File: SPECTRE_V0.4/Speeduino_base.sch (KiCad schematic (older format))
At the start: 160 parts, among them IC1 LM340?-MP, Q1 2N7002, Q10 BSP78, Q11 BSP78, Q12 BSP78, Q13 BSP78, Q2 CJ2302, Q3 CJ2302, Q4 CJ2302, Q5 BSP78, Q6 BSP78, Q7 CJ2302, Q8 CJ2302, Q9 CJ2302, U1 MAX9926UAEE+, U2 molex_48pin

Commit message: Cleaned up V0.4 Bug fixes in board V0.4 Changed readme to add more to be tested functions
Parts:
- removed L1: 470R-2A, Speeduino_base:L0805, symbol Speeduino_base-eagle-import:SMD-FERRITE-BEAD-470R-2A(0805)'0805'
- added D22, D23, D24, D25: 1N4007, Diode_SMD:D_SOD-128, symbol Device:D_Small
- added J1: Conn_01x04_Male, Connector_PinHeader_2.54mm:PinHeader_1x04_P2.54mm_Vertical, symbol Connector:Conn_01x04_Male
- added R72: 0R0, Resistor_SMD:R_0603_1608Metric_Pad1.05x0.95mm_HandSolder, symbol Speeduino_base-eagle-import:SMD-RES-470R-5%-1_10W(0603)
- added R73, R74: 1k, Speeduino_base:R0603, symbol Speeduino_base-eagle-import:SMD-RES-470R-5%-1_10W(0603)
- R69: value 1k -> 180
- R70: value 1k -> 82
- R71: value 1k -> 560
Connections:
- wire segments 540 -> 548
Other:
- moved on the sheet: D1, D4, R13, R4

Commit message: Lots of changes, started new PCB with 8 inj channels.
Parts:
- removed F3, F4: PPTC 16V2A, Speeduino_base:1812L, symbol Speeduino_base-eagle-import:?1812L
- removed F5, F6, F7: PPTC 16V2A, Fuse:Fuse_1812_4532Metric, symbol Device:Polyfuse_Small
- removed IC1: LM340?-MP, Speeduino_base:SOT223, symbol Speeduino_base-eagle-import:LM340?-MP
- removed JP15, JP5, JP6, JP7, JP8: SolderJumper_3_Bridged12, Jumper:SolderJumper-3_P1.3mm_Bridged12_Pad1.0x1.5mm, symbol Jumper:SolderJumper_3_Bridged12
- removed U$1: A4988BREAKOUT, Speeduino_base:A4988BREAKOUT, symbol Speeduino_base-eagle-import:A4988BREAKOUT
- added A1: Pololu_Breakout_DRV8825, Module:Pololu_Breakout-16_15.2x20.3mm, symbol Driver_Motor:Pololu_Breakout_DRV8825
- added D26: 1N4007, Diode_SMD:D_SOD-128, symbol Device:D_Small
- added F2: PPTC 16V2A, Resistor_SMD:R_1812_4532Metric_Pad1.30x3.40mm_HandSolder, symbol Speeduino_base-eagle-import:?1812L
- added Q14, Q15, Q16, Q17, Q18: BSP78, Speeduino_base:SOT223, symbol Speeduino_base-eagle-import:NMOSSOT223
- added R75, R76: 10k, Resistor_SMD:R_0603_1608Metric_Pad1.05x0.95mm_HandSolder, symbol Device:R_Small
- added R77: 100, Speeduino_base:R0603, symbol Speeduino_base-eagle-import:SMD-RES-470R-5%-1_10W(0603)
- added R78, R79, R80, R81, R82: 10k, Speeduino_base:R0603, symbol Speeduino_base-eagle-import:SMD-RES-470R-5%-1_10W(0603)
- added U3: LM78M05_TO220, Package_TO_SOT_THT:TO-220-3_Vertical, symbol Regulator_Linear:LM78M05_TO220
- F1: footprint Speeduino_base:1812L -> Resistor_SMD:R_1812_4532Metric_Pad1.30x3.40mm_HandSolder
- J1: footprint Connector_PinHeader_2.54mm:PinHeader_1x04_P2.54mm_Vertical -> Connector_PinHeader_2.00mm:PinHeader_1x04_P2.00mm_Vertical_SMD_Pin1Left
- R2: footprint Speeduino_base:R0603 -> Resistor_SMD:R_0603_1608Metric_Pad1.05x0.95mm_HandSolder
- R23: footprint Speeduino_base:R-7,5 -> Varistor:RV_Disc_D12mm_W3.9mm_P7.5mm
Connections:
- net labels added: BOOST-OUT, INJ5-OUT, INJ6-OUT, INJ7-OUT, INJ8-OUT
- net labels removed: Baro, PA11, PA12, PA15, PA6, PA7, PB0, PC10, PC11, PC12, PC9, PD2, VREF+, VREF-, V_IGN, V_INJ12, V_INJ34, V_O2
- wire segments 548 -> 476
- no-connect marks 0 -> 50
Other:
- moved on the sheet: C1, C10, C12, C14, C15, C16, C17, C18, C19, C2, C20, C21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

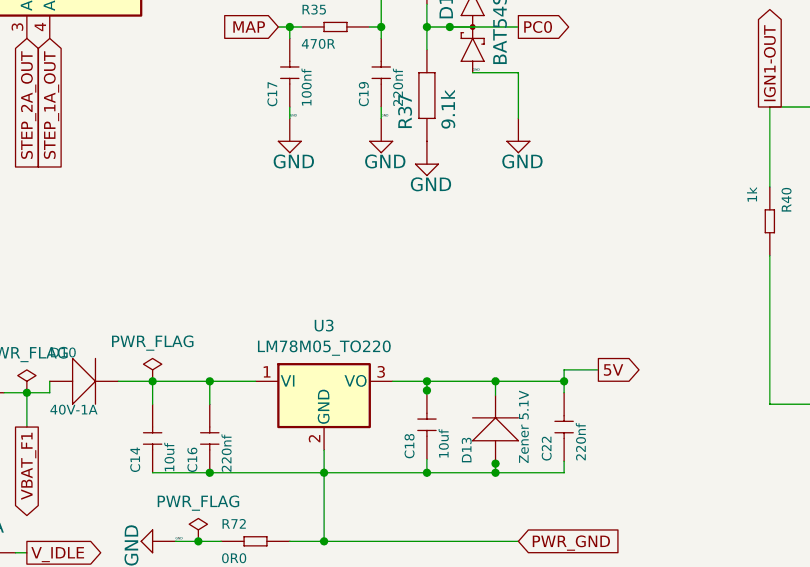
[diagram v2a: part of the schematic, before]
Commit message: Add zener for safety on 3.3v. All bat54S diodes dump current on 3.3V line when driven above 3.6V therefor the 3.3V needed protection
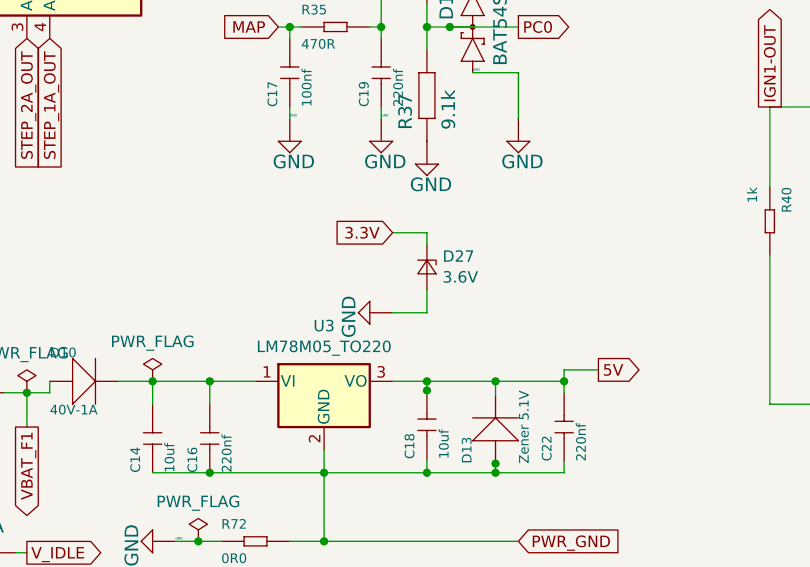
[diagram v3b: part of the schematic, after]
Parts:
- added D27: 3.6V, Diode_SMD:D_MiniMELF_Handsoldering, symbol Device:D_Zener_Small
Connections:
- wire segments 476 -> 480
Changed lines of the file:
@@
 Text GLabel 11750 3400 0    50   BiDi ~ 0
 PB7
-Text GLabel 11750 3500 0    50   BiDi ~ 0
-PB5
 Text GLabel 11750 3600 0    50   BiDi ~ 0
 PD7
@@
 Text GLabel 12050 3400 2    50   BiDi ~ 0
 PB6
-Text GLabel 12050 3500 2    50   BiDi ~ 0
-PB3
 Text GLabel 12050 3600 2    50   BiDi ~ 0
 PD6
@@
 NoConn ~ 10500 4800
 NoConn ~ 10500 4900
+$Comp
+L Device:D_Zener_Small D27
+U 1 1 5E7D198A
+P 3150 10300
+F 0 "D27" V 3104 10368 50  0000 L CNN
+F 1 "3.6V" V 3195 10368 50  0000 L CNN
+F 2 "Diode_SMD:D_MiniMELF_Handsoldering" V 3150 10300 50  0001 C CNN
+F 3 "~" V 3150 10300 50  0001 C CNN
+	1    3150 10300
+	0    1    1    0
+$EndComp
+Wire Wire Line
+	3150 10200 3150 10150
+Wire Wire Line
+	3150 10150 3000 10150
+Wire Wire Line
+	3150 10400 3150 10500
+Wire Wire Line
+	3150 10500 3000 10500
+$Comp
+L Speeduino_base-eagle-import:GND #SUPPLY0108
+U 1 1 5E8517DF
+P 2900 10500
+F 0 "#SUPPLY0108" H 2900 10500 50  0001 C CNN
+F 1 "GND" H 2825 10375 59  0000 L BNN
+F 2 "" H 2900 10500 50  0001 C CNN
+F 3 "" H 2900 10500 50  0001 C CNN
+	1    2900 10500
+	0    1    1    0
+$EndComp
+Text GLabel 3000 10150 0    50   Input ~ 0
+3.3V
+Text GLabel 11750 3500 0    50   BiDi ~ 0
+PB5
+Text GLabel 12050 3500 2    50   BiDi ~ 0
+PB3
 $EndSCHEMATC

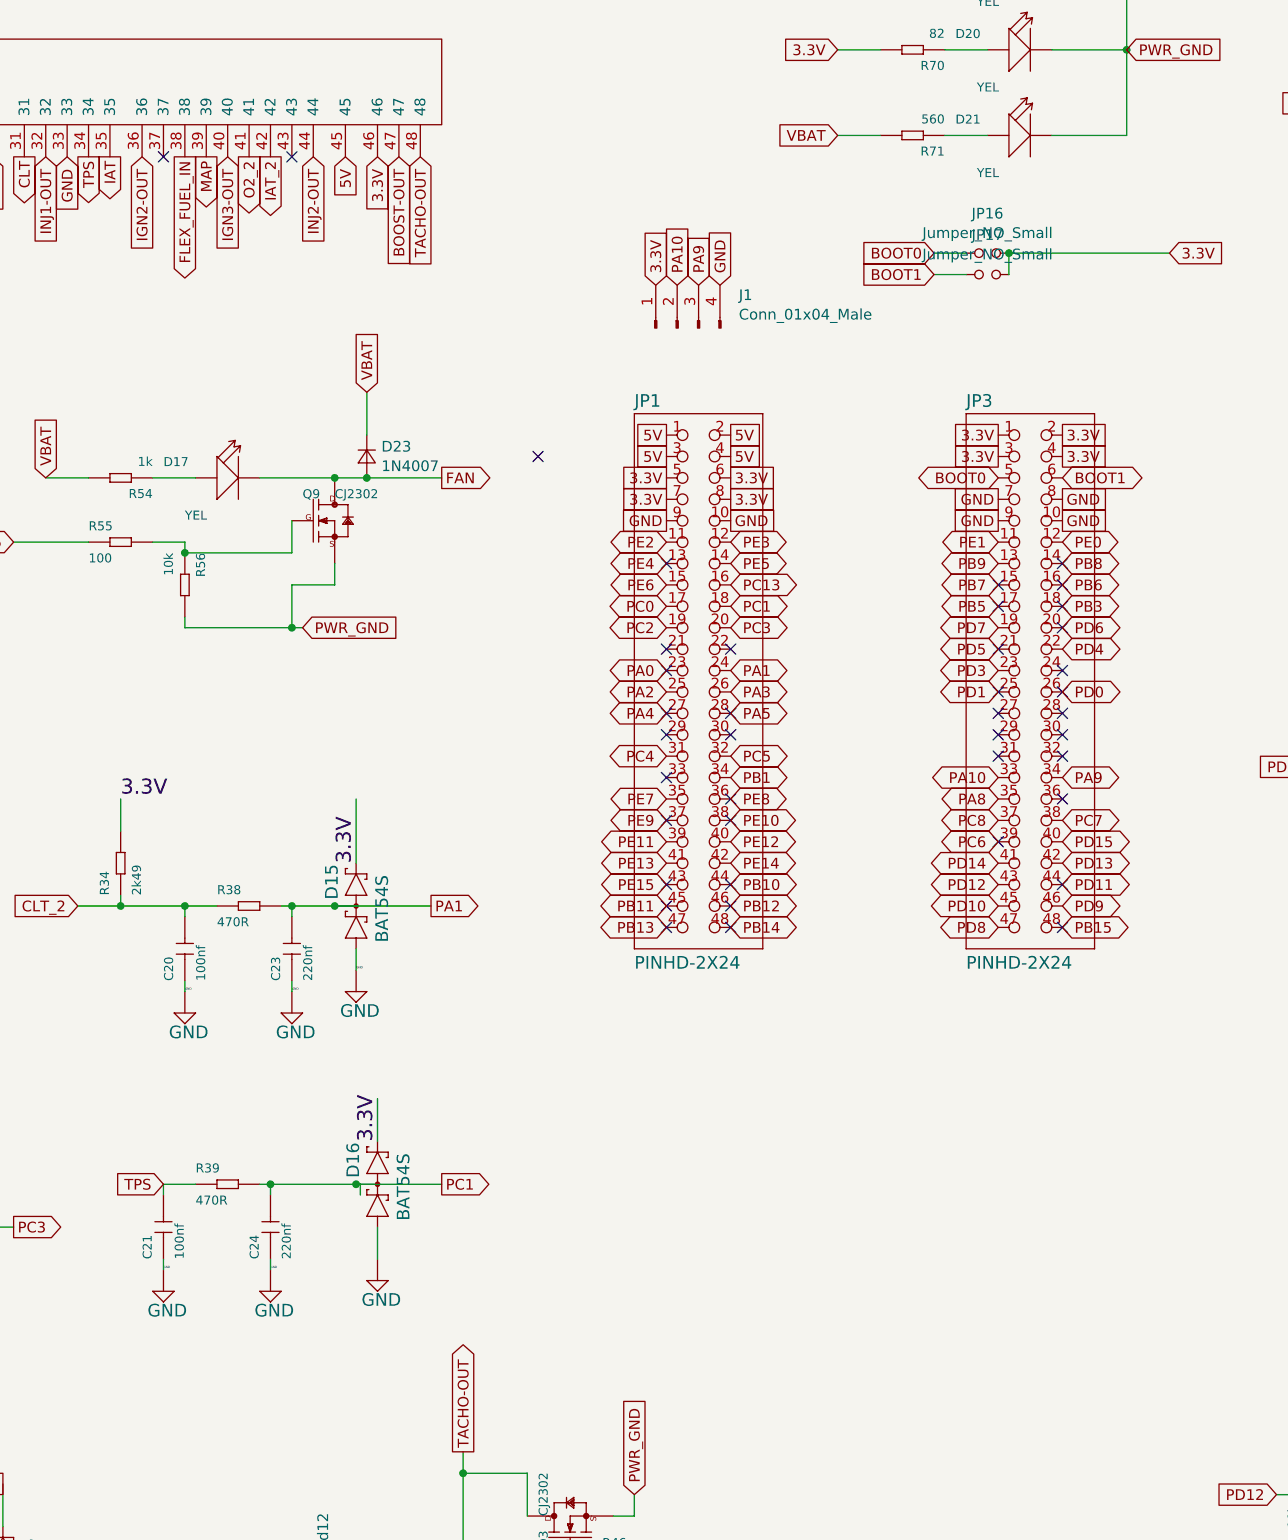
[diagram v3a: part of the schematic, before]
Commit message: add canbus driver add 3d models to components for 3d render.
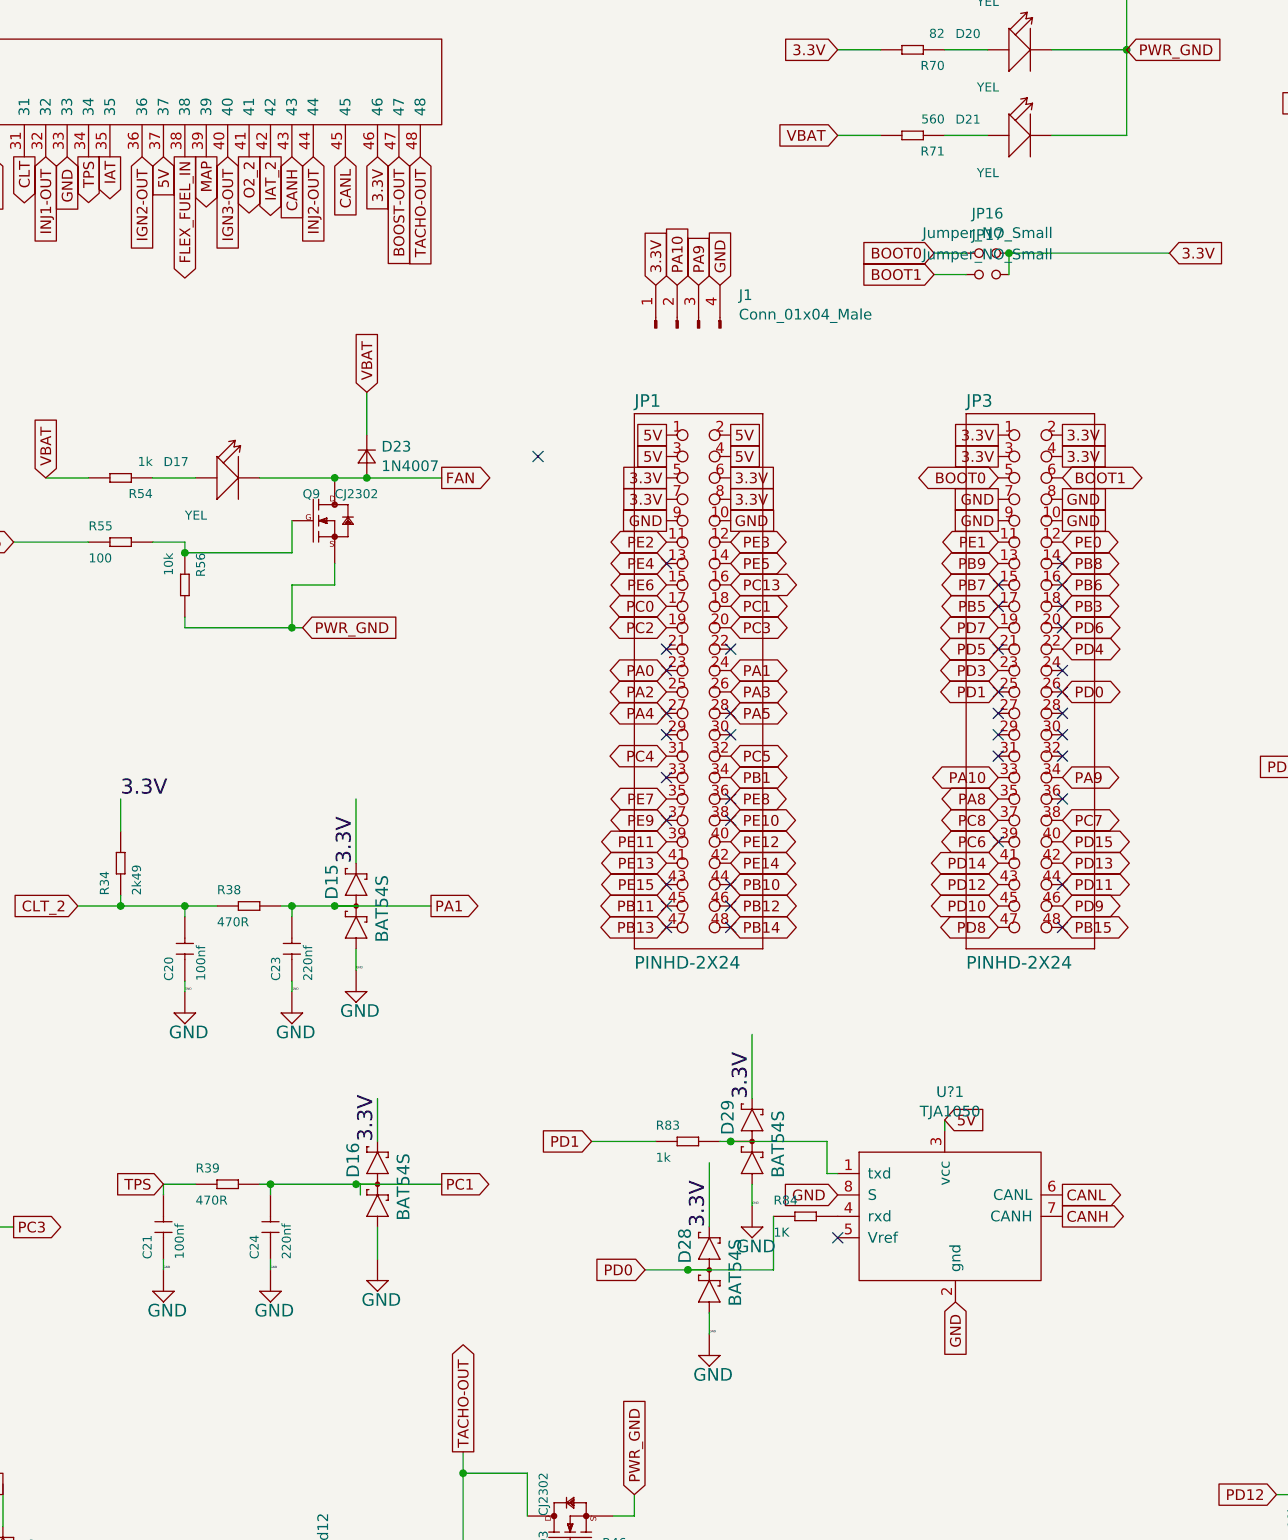
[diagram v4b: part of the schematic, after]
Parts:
- added D28, D29: BAT54S, Speeduino_base:SOT23, symbol Speeduino_base-eagle-import:BAT54S
- added R83: 1k, Speeduino_base:R0603, symbol Speeduino_base-eagle-import:SMD-RES-470R-5%-1_10W(0603)
- added R84: 1K, Speeduino_base:R0603, symbol Speeduino_base-eagle-import:SMD-RES-470R-5%-1_10W(0603)
- added U?1: TJA1050, Package_SO:SO-8_5.3x6.2mm_P1.27mm, symbol speeduino_lib:TJA1050
- D22, D23, D24, D25, D26: footprint Diode_SMD:D_SOD-128 -> Speeduino_base:D_SOD-128
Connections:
- net labels added: CANH, CANL
- wire segments 480 -> 493
- no-connect marks 50 -> 49
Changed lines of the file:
@@
-$EndComp
-$Comp
-L Speeduino_base-eagle-import:BAT54S D15
-U 1 1 20478EC3
-P 8750 4900
-F 0 "D15" H 8780 4979 59  0000 L BNN
-F 1 "BAT54S" H 8580 4744 59  0000 L BNN
-F 2 "Speeduino_base:SOT23" H 8750 4900 50  0001 C CNN
-F 3 "" H 8750 4900 50  0001 C CNN
-	1    8750 4900
-	0    -1   -1   0
 $EndComp
 $Comp
@@
 Text GLabel 5050 1400 3    50   Input ~ 0
 STEP_1B_OUT
-Text GLabel 8700 1400 3    50   Input ~ 0
+Text GLabel 7850 1400 3    50   Input ~ 0
 5V
 Text GLabel 8050 1400 3    50   Output ~ 0
 MAP
-Connection ~ 4200 1400
-$Comp
-L molex_48pin:molex_48pin U2
-U 1 1 5E17AB54
-P 6900 1950
-F 0 "U2" V 8187 2355 60  0000 C CNN
-F 1 "molex_48pin" V 8081 2355 60  0000 C CNN
-F 2 "rusefi_lib:Molex_48" H 6900 1950 60  0001 C CNN
-F 3 "" H 6900 1950 60  0001 C CNN
-	1    6900 1950
-	0    -1   -1   0
-$EndComp
 Text GLabel 7050 1400 3    50   Input ~ 0
 GND
@@
 F 0 "D24" V 14654 2418 50  0000 L CNN
 F 1 "1N4007" V 14745 2418 50  0000 L CNN
-F 2 "Diode_SMD:D_SOD-128" V 14700 2350 50  0001 C CNN
+F 2 "Speeduino_base:D_SOD-128" V 14700 2350 50  0001 C CNN
 F 3 "~" V 14700 2350 50  0001 C CNN
 	1    14700 2350
@@
 F 0 "D25" V 14654 3918 50  0000 L CNN
 F 1 "1N4007" V 14745 3918 50  0000 L CNN
-F 2 "Diode_SMD:D_SOD-128" V 14700 3850 50  0001 C CNN
+F 2 "Speeduino_base:D_SOD-128" V 14700 3850 50  0001 C CNN
 F 3 "~" V 14700 3850 50  0001 C CNN
 	1    14700 3850
@@
 F 0 "D22" V 5554 3368 50  0000 L CNN
 F 1 "1N4007" V 5645 3368 50  0000 L CNN
-F 2 "Diode_SMD:D_SOD-128" V 5600 3300 50  0001 C CNN
+F 2 "Speeduino_base:D_SOD-128" V 5600 3300 50  0001 C CNN
 F 3 "~" V 5600 3300 50  0001 C CNN
 	1    5600 3300
@@
 F 0 "D23" V 8754 2868 50  0000 L CNN
 F 1 "1N4007" V 8845 2868 50  0000 L CNN
-F 2 "Diode_SMD:D_SOD-128" V 8800 2800 50  0001 C CNN
+F 2 "Speeduino_base:D_SOD-128" V 8800 2800 50  0001 C CNN
 F 3 "~" V 8800 2800 50  0001 C CNN
 	1    8800 2800
@@
 F 0 "D26" V 14504 818 50  0000 L CNN
 F 1 "1N4007" V 14595 818 50  0000 L CNN
-F 2 "Diode_SMD:D_SOD-128" V 14550 750 50  0001 C CNN
+F 2 "Speeduino_base:D_SOD-128" V 14550 750 50  0001 C CNN
 F 3 "~" V 14550 750 50  0001 C CNN
 	1    14550 750
@@
 	1    0    0    -1
 $EndComp
-NoConn ~ 8450 1400
-NoConn ~ 7850 1400
 NoConn ~ 5750 1400
 NoConn ~ 10200 4000
@@
 Text GLabel 12050 3500 2    50   BiDi ~ 0
 PB3
+$Comp
+L speeduino_lib:TJA1050 U?1
+U 1 1 5E827D30
+P 11600 6400
+F 0 "U?1" H 11525 7031 50  0000 C CNN
+F 1 "TJA1050" H 11525 6940 50  0000 C CNN
+F 2 "Package_SO:SO-8_5.3x6.2mm_P1.27mm" H 11600 6400 50  0001 C CNN
+F 3 "" H 11600 6400 50  0001 C CNN
+	1    11600 6400
+	1    0    0    -1
+$EndComp
+NoConn ~ 11000 6450
+Text GLabel 12050 6250 2    50   Output ~ 0
+CANL
+Text GLabel 12050 6350 2    50   Output ~ 0
+CANH
+Connection ~ 4200 1400
+$Comp
+L molex_48pin:molex_48pin U2
+U 1 1 5E17AB54
+P 6900 1950
+F 0 "U2" V 8187 2355 60  0000 C CNN
+F 1 "molex_48pin" V 8081 2355 60  0000 C CNN
+F 2 "rusefi_lib:Molex_48" H 6900 1950 60  0001 C CNN
+F 3 "" H 6900 1950 60  0001 C CNN
+	1    6900 1950
+	0    -1   -1   0
+$EndComp
+Text GLabel 8450 1400 3    50   Input ~ 0
+CANH
+Text GLabel 8700 1400 3    50   Input ~ 0
+CANL
+Text GLabel 11500 5900 2    50   Input ~ 0
+5V
+Wire Wire Line
+	11500 5900 11500 5950
+Text GLabel 10100 6600 0    50   Input ~ 0
+PD0
+Text GLabel 9850 6000 0    50   Input ~ 0
+PD1
+Text GLabel 11550 6750 3    50   Input ~ 0
+GND
+Text GLabel 11000 6250 0    50   Input ~ 0
+GND
+Wire Wire Line
+	10600 6300 10600 6200
+Text Label 10600 6300 0    10   ~ 0
+GND
+Wire Wire Line
+	10600 5800 10600 5500
+Text Label 10600 5800 1    70   ~ 0
+3.3V
+$Comp
+L Speeduino_base-eagle-import:GND #SUPPLY0109
+U 1 1 5E8B962B
+P 10600 6400
+F 0 "#SUPPLY0109" H 10600 6400 50  0001 C CNN
+F 1 "GND" H 10525 6275 59  0000 L BNN
+F 2 "" H 10600 6400 50  0001 C CNN
+F 3 "" H 10600 6400 50  0001 C CNN
+	1    10600 6400
+	1    0    0    -1
+$EndComp
+Wire Wire Line
+	10950 6000 10950 6150
+Wire Wire Line
+	10950 6150 11000 6150
+Wire Wire Line
+	10400 6900 10400 6800
+Text Label 10400 6900 0    10   ~ 0
+GND
+Wire Wire Line
+	10400 6400 10400 6100
+Text Label 10400 6400 1    70   ~ 0
+3.3V
+$Comp
+L Speeduino_base-eagle-import:GND #SUPPLY0110
+U 1 1 5E93B03C
+P 10400 7000
+F 0 "#SUPPLY0110" H 10400 7000 50  0001 C CNN
+F 1 "GND" H 10325 6875 59  0000 L BNN
+F 2 "" H 10400 7000 50  0001 C CNN
+F 3 "" H 10400 7000 50  0001 C CNN
+	1    10400 7000
+	1    0    0    -1
+$EndComp
+$Comp
+L Speeduino_base-eagle-import:BAT54S D28
+U 1 1 5E93B042
+P 10400 6600
+F 0 "D28" H 10430 6679 59  0000 L BNN
+F 1 "BAT54S" H 10230 6444 59  0000 L BNN
+F 2 "Speeduino_base:SOT23" H 10400 6600 50  0001 C CNN
+F 3 "" H 10400 6600 50  0001 C CNN
+	1    10400 6600
+	0    -1   -1   0
+$EndComp
+Wire Wire Line
+	10100 6600 10300 6600
+Connection ~ 10300 6600
+$Comp
+L Speeduino_base-eagle-import:SMD-RES-470R-5%-1_10W(0603) R84
+U 1 1 5E97C8A6
+P 10850 6350
+F 0 "R84" H 10700 6400 42  0000 L BNN
+F 1 "1K" H 10700 6250 42  0000 L BNN
+F 2 "Speeduino_base:R0603" H 10850 6350 50  0001 C CNN
+F 3 "" H 10850 6350 50  0001 C CNN
+	1    10850 6350
+	1    0    0    -1
+$EndComp
+$Comp
+L Speeduino_base-eagle-import:SMD-RES-470R-5%-1_10W(0603) R83
+U 1 1 5E97D64D
+P 10300 6000
+F 0 "R83" H 10150 6050 42  0000 L BNN
+F 1 "1k" H 10150 5900 42  0000 L BNN
+F 2 "Speeduino_base:R0603" H 10300 6000 50  0001 C CNN
+F 3 "" H 10300 6000 50  0001 C CNN
+	1    10300 6000
+	1    0    0    -1
+$EndComp
+Wire Wire Line
+	10450 6000 10500 6000
+Connection ~ 10500 6000
+Wire Wire Line
+	10500 6000 10950 6000
+Wire Wire Line
+	10150 6000 9850 6000
+Wire Wire Line
+	10700 6350 10700 6600
+Wire Wire Line
+	10300 6600 10700 6600
+$Comp
+L Speeduino_base-eagle-import:BAT54S D15
+U 1 1 20478EC3
+P 8750 4900
+F 0 "D15" H 8780 4979 59  0000 L BNN
+F 1 "BAT54S" H 8580 4744 59  0000 L BNN
+F 2 "Speeduino_base:SOT23" H 8750 4900 50  0001 C CNN
+F 3 "" H 8750 4900 50  0001 C CNN
+	1    8750 4900
+	0    -1   -1   0
+$EndComp
+$Comp
+L Speeduino_base-eagle-import:BAT54S D29
+U 1 1 5E8B9631
+P 10600 6000
+F 0 "D29" H 10630 6079 59  0000 L BNN
+F 1 "BAT54S" H 10430 5844 59  0000 L BNN
+F 2 "Speeduino_base:SOT23" H 10600 6000 50  0001 C CNN
+F 3 "" H 10600 6000 50  0001 C CNN
+	1    10600 6000
+	0    -1   -1   0
+$EndComp
 $EndSCHEMATC
